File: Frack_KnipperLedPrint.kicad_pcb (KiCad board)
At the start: 2 copper layers, 40 x 50 mm, 15 parts, among them J1 Conn_01x01, J2 Conn_01x01, Q1 BC547, Q2 BC547

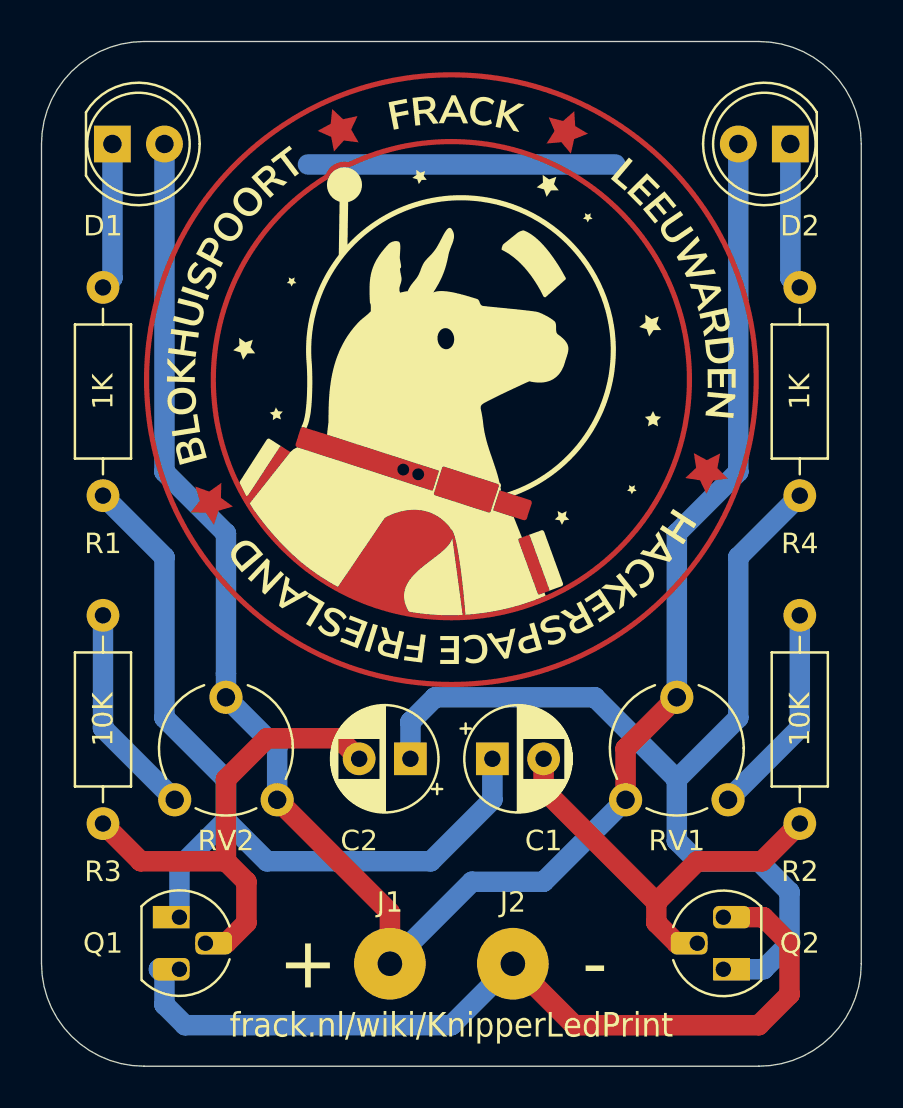
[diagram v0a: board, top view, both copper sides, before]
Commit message: Annotations and render
Changed annotations to match old design
Added 3d model of potentiometer
Added render images of pcb
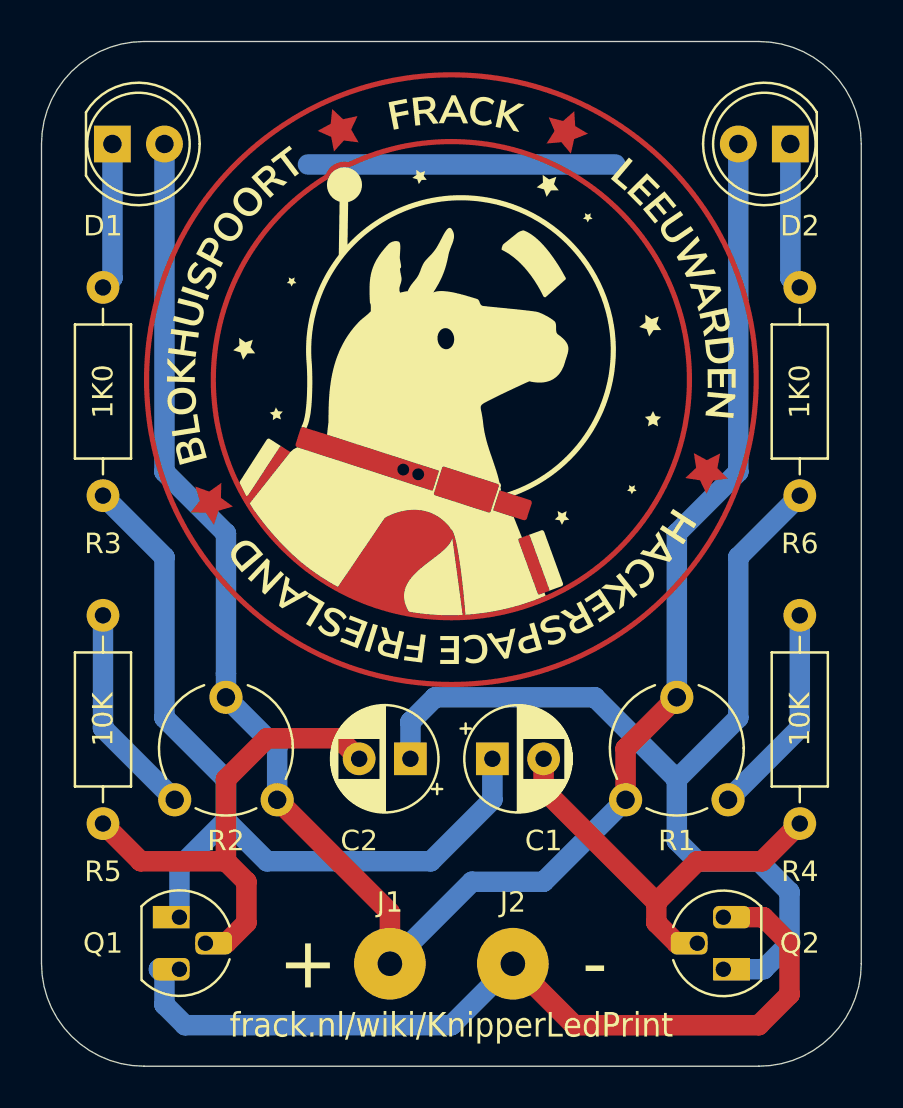
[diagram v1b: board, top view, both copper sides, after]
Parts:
- removed RV1, RV2: 250K, Potentiometer_THT:Potentiometer_Piher_PT-6-V_Vertical
- added R1: 250K, Custom_parts:Potentiometer_Piher_PT-6-V_Vertical, F.Cu at (33.5, 37.0)
- added R2: 250K, Custom_parts:Potentiometer_Piher_PT-6-V_Vertical, F.Cu at (11.5, 37.0)
- R3: renamed from R1; value 1K -> 1K0
- R6: renamed from R4; value 1K -> 1K0
- renumbered R2 to R4, R3 to R5
